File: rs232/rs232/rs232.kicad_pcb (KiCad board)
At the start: 2 copper layers, 59 x 64.1 mm, 25 parts, among them J1 Conn_01x03_Pin, J2 Conn_01x04_Pin, J3 Conn_01x03_Pin, J4 Conn_01x02_Pin

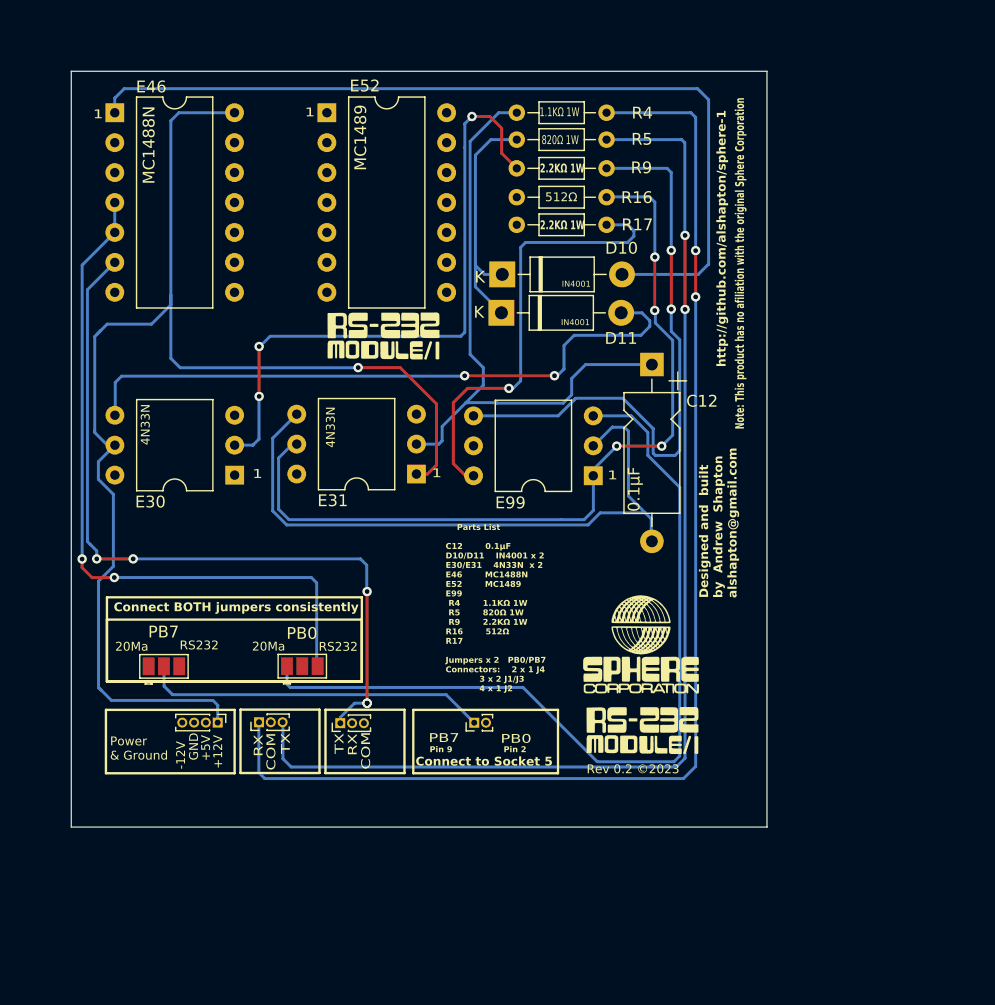
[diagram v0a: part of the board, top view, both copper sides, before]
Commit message: Updated gitignore
Now ignores backup files
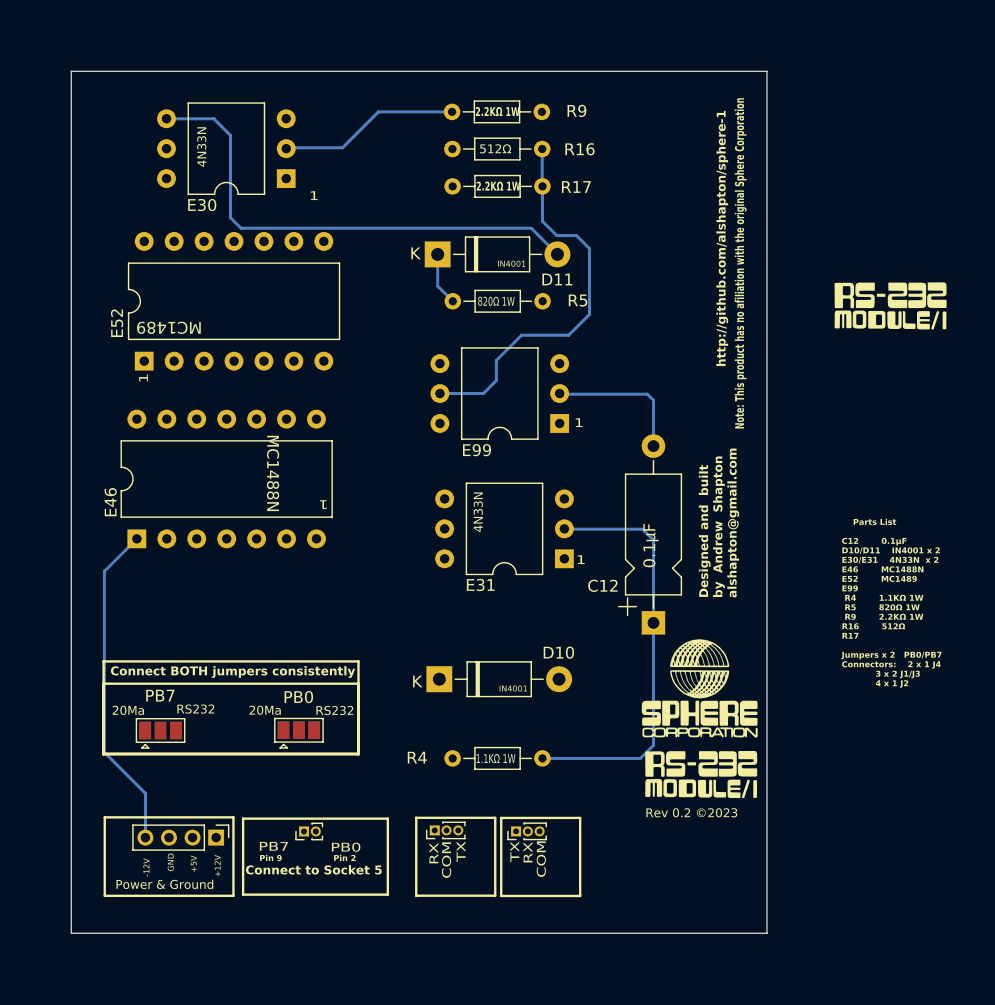
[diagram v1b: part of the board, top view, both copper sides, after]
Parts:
- J2: footprint Connector_PinHeader_1.00mm:PinHeader_1x04_P1.00mm_Vertical -> Connector_PinHeader_2.00mm:PinHeader_1x04_P2.00mm_Vertical
- moved R4 54.8 mm to (108.3, 88.8), turned to 180 degrees
- moved G*** 43.1 mm to (137.8, 50.4)
- moved E46 36.2 mm to (73.9, 70.2), turned to 90 degrees
- moved D10 34.8 mm to (99.5, 82.1)
- moved E52 26.2 mm to (74.5, 55.1), turned to 90 degrees
- moved E30 25.5 mm to (86.5, 39.6)
- moved C12 21.9 mm to (117.7, 77.3), turned to 90 degrees
- moved J1 17.5 mm to (99.2, 94.9)
- moved J3 17.5 mm to (106.0, 95.0)
- moved J4 17.1 mm to (88.1, 95.0)
- moved R5 14.8 mm to (100.7, 50.0)
- moved E31 14.5 mm to (110.2, 71.8)
- moved R16 13.7 mm to (100.7, 37.1), turned to 0 degrees
- moved R17 13.5 mm to (100.7, 40.2), turned to 0 degrees
- moved J2 9.76 mm to (80.6, 95.5)
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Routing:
- net Net-(E31-A): track 111.9 -> 0.00 mm, vias 1 -> 0
- net Net-(J1-Pin_1): track 104.8 -> 0.03 mm, vias 2 -> 0
- net Net-(J1-Pin_3): track 96.9 -> 0.04 mm, vias 2 -> 0
- net Net-(E99-2A): track 71.6 -> 0.00 mm
- net Net-(E99-1A): track 70.0 -> 0.00 mm, vias 4 -> 0
- net Net-(E46-2Y): track 64.6 -> 0.00 mm, vias 5 -> 0
- net Net-(E46-2A): track 59.5 -> 0.00 mm, vias 2 -> 0
- net Net-(E99-2Y): track 51.2 -> 0.00 mm, vias 2 -> 0
- net Net-(D10-A): track 74.5 -> 28.5 mm
- net Net-(E31-E): track 56.4 -> 12.1 mm
- net Net-(E30-C-Pad2): track 53.5 -> 15.4 mm, vias 3 -> 0
- net Net-(E99-1Y): track 38.1 -> 0.00 mm, vias 1 -> 0
- net Net-(E30-A): track 0.06 -> 33.1 mm
- net Net-(J4-Pin_1): track 29.4 -> 0.44 mm
- net Net-(C12-Pad1): track 52.6 -> 35.3 mm
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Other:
- board size 59 x 64.1 mm -> 59 x 73.1 mm

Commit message: Final commit before disassociating from combined repo
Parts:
- removed the G*** at (137.8, 50.4)
- removed the G*** at (161.7, 152.5)
- added H1: MountingHole_Pad, MountingHole:MountingHole_3.7mm_Pad_Via, F.Cu at (114.9, 113.4)
- added H2: MountingHole_Pad, MountingHole:MountingHole_3.7mm_Pad_Via, F.Cu at (114.3, 26.1)
- added H3: MountingHole_Pad, MountingHole:MountingHole_3.7mm_Pad_Via, F.Cu at (21.4, 25.8)
- added H4: MountingHole_Pad, MountingHole:MountingHole_3.7mm_Pad_Via, F.Cu at (21.4, 113.7)
- added J5: X5 Pass Through, Package_DIP:DIP-14_W10.16mm, F.Cu at (84.8, 105.0)
- added J6: Conn_01x03_Pin, Connector_PinHeader_2.54mm:PinHeader_1x07_P2.54mm_Vertical, B.Cu at (52.7, 105.0)
- E30, E31, E99: footprint Package_DIP:DIP-6_W10.16mm -> Package_DIP:DIP-6_W7.62mm
- J1, J3: footprint Connector_PinHeader_1.00mm:PinHeader_1x03_P1.00mm_Vertical -> Connector_PinHeader_2.54mm:PinHeader_1x03_P2.54mm_Vertical
- J2: footprint Connector_PinHeader_2.00mm:PinHeader_1x04_P2.00mm_Vertical -> Connector_PinHeader_2.54mm:PinHeader_1x04_P2.54mm_Vertical
- J4: value Conn_01x02_Pin -> Conn_01x03_Pin; footprint Connector_PinHeader_1.00mm:PinHeader_1x02_P1.00mm_Vertical -> Connector_PinHeader_2.54mm:PinHeader_1x07_P2.54mm_Vertical; moved to B.Cu
- PB0, PB7: footprint Jumper:SolderJumper-3_P1.3mm_Open_Pad1.0x1.5mm -> Connector_PinHeader_2.54mm:PinHeader_1x03_P2.54mm_Vertical
- R16, R17, R4, R5, R9: footprint Resistor_THT:R_Axial_DIN0204_L3.6mm_D1.6mm_P7.62mm_Horizontal -> Resistor_THT:R_Axial_DIN0414_L11.9mm_D4.5mm_P25.40mm_Horizontal
- moved G*** 156.7 mm to (130.0, 170.8)
- moved G*** 141.4 mm to (129.9, 178.0)
- moved G*** 101.6 mm to (32.6, 41.4)
- moved G*** 101.5 mm to (32.6, 34.2)
- moved J3 86.6 mm to (28.2, 57.0), turned to 0 degrees
- moved J1 74.8 mm to (28.3, 71.0), turned to 0 degrees
- moved E31 69.7 mm to (47.6, 41.2), turned to 90 degrees
- moved D10 54.5 mm to (62.0, 42.6), turned to 90 degrees
- moved J2 52.1 mm to (28.5, 93.9), turned to 180 degrees
- moved E99 47.1 mm to (76.0, 93.2), turned to 90 degrees
- moved E30 45.3 mm to (47.6, 62.8), turned to 90 degrees
- moved J4 40.7 mm to (52.8, 115.2)
- moved D11 38.0 mm to (62.1, 53.6), turned to -90 degrees
- moved E52 34.4 mm to (48.0, 77.1)
- moved E46 34.3 mm to (48.2, 93.0)
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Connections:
- J4 pad 1: Net-(J4-Pin_1) -> Net-(J5-Pin_7)
- J4 pad 2: Net-(J4-Pin_2) -> Net-(J5-Pin_6)
- PB0 pad 2: Net-(J4-Pin_2) -> Net-(J5-Pin_2)
- PB7 pad 2: Net-(J4-Pin_1) -> Net-(J5-Pin_9)
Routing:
- net Net-(E31-E): track 12.1 -> 222.5 mm, vias 0 -> 5
- net Net-(E30-A): track 33.1 -> 193.9 mm, vias 0 -> 2
- net Net-(E99-1A): track 0.00 -> 115.4 mm, vias 0 -> 2
- net Net-(D10-A): track 28.5 -> 136.3 mm, vias 0 -> 2
- net Net-(J1-Pin_3): track 0.04 -> 103.0 mm
- net Net-(E99-1Y): track 0.00 -> 102.5 mm, vias 0 -> 2
- net Net-(E46-2Y): track 0.00 -> 94.7 mm
- net Net-(E99-2Y): track 0.00 -> 83.4 mm
- net Net-(E31-A): track 0.00 -> 77.4 mm, vias 0 -> 3
- net Net-(E52-1Y): track 0.00 -> 77.2 mm, vias 0 -> 2
- net Net-(J5-Pin_2): track 0.00 -> 66.9 mm
- net Net-(C12-Pad1): track 35.3 -> 98.3 mm, vias 0 -> 2
- net Net-(J5-Pin_1): track 0.00 -> 58.8 mm
- net Net-(J5-Pin_9): track 0.00 -> 58.1 mm
- net Net-(E46-2A): track 0.00 -> 58.0 mm
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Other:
- board size 59 x 73.1 mm -> 104 x 100.7 mm
- board text added: "(E40)"
- board text added: "14"
- board text added: "7"
- board text added: "8"
- board text added: "BATCH: OID(B-${FAB_PLANT_USER}/${CURRENT_DATE}/WayWayWay/)"
- board text added: "Parts List C12 0.1µF D10/D11 IN4001 x 2 E30/E31 4N33N x 2 E46 MC1488N E52 MC1489 E99(E40) SN7404 R4 1.1KΩ 1W R5 820Ω 1W R9 2.2KΩ 1W R16 512Ω R1 72.2KΩ 1W Jumpers x 2 PB0/PB7 Connectors: 2 x 1 J4 3 x 2 J1/J3 4 x 1 J2"
- board text added: "Rev B ©2024"
- board text added: "SERIAL NUMBER : ARC/0.2/__________________________"
- board text added: "SN7404"
- board text added: "X5 Connection"
- board text added: "https://github.com/Sphere-Corporation"
- board text added: "}"
- board text removed: "Connect to Socket 5"
- board text removed: "OID : ${FAB_PLANT_USER}/${CURRENT_DATE}/WayWayWay"
- board text removed: "PB0"
- board text removed: "PB7"
- board text removed: "Parts List C12 0.1µF D10/D11 IN4001 x 2 E30/E31 4N33N x 2 E46 MC1488N E52 MC1489 E99 R4 1.1KΩ 1W R5 820Ω 1W R9 2.2KΩ 1W R16 512Ω R17 Jumpers x 2 PB0/PB7 Connectors: 2 x 1 J4 3 x 2 J1/J3 4 x 1 J2"
- board text removed: "Pin 2"
- board text removed: "Pin 9"
- board text removed: "Rev 0.2 ©2023"
- board text removed: "http://github.com/alshapton/sphere-1"
